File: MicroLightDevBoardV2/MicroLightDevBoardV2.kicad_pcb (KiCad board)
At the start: 2 copper layers, 58 parts, among them J1 Conn_01x05_Socket, J10 Conn_01x01_Socket, J11 Conn_01x04_Socket, J12 Conn_01x05_Socket, J13 Conn_01x02_Socket, J14 Conn_01x04_Socket, J15 Conn_01x04_Socket, J16 Conn_01x05_Socket, J17 Conn_01x01_Socket, J18 Conn_01x03_Socket, J19 Conn_01x03_Socket, J2 Conn_01x05_Socket, J20 Conn_01x02_Socket, J21 Conn_01x02_Socket, J22 Conn_01x02_Socket, J23 Conn_01x02_Socket, J24 Conn_01x01_Socket, J25 Conn_01x06_Socket, J26 Conn_01x04_Socket, J3 Conn_01x05_Socket, J4 Conn_01x05_Socket, J5 Conn_01x02_Socket, J6 Conn_01x02_Socket, J7 TYPE-C-31-M-12, J8 Conn_01x02_Socket, J9 Conn_01x02_Socket, U1 BQ25628RYKR, U2 ATtiny3226-M, U3 S-85S1AB33-I6T1U, U4 USBLC6-2P6, U5 MC3479

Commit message: organizing on pcb
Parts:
- moved J12 41.3 mm to (132.3, 30.7)
- moved J15 35.2 mm to (128.1, 44.9), turned to 90 degrees
- moved J17 33.8 mm to (153.9, 44.7)
- moved J5 33.1 mm to (151.4, 36.1), turned to 90 degrees
- moved R2 28.7 mm to (145.9, 37.2)
- moved R3 26.6 mm to (146.0, 39.7)
- moved J6 26.3 mm to (151.4, 39.8), turned to 90 degrees
- moved U1 26.2 mm to (131.4, 39.7)
- moved C4 26.0 mm to (137.2, 39.7), turned to -90 degrees
- moved C1 24.3 mm to (128.3, 38.0), turned to -90 degrees
- moved C3 24.0 mm to (135.7, 39.7), turned to -90 degrees
- moved R1 23.2 mm to (145.9, 42.3)
- moved J13 23.2 mm to (123.4, 30.7), turned to 90 degrees
- moved J14 21.9 mm to (123.4, 35.8)
- moved J16 14.1 mm to (142.6, 34.6)
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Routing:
- net GND_CHRG: track 0.00 -> 53.5 mm, vias 0 -> 2
- net VREF_CHRG: track 0.00 -> 32.7 mm
- net SCL_CHRG: track 0.00 -> 20.3 mm, vias 0 -> 1
- net SDA_CHRG: track 0.00 -> 19.4 mm
- net INT: track 0.00 -> 13.2 mm, vias 0 -> 1
- net SYS: track 0.00 -> 13.1 mm
- net VBUS_CHRG: track 0.00 -> 12.5 mm
- net STAT: track 0.00 -> 11.9 mm, vias 0 -> 1
- net CE: track 0.00 -> 11.7 mm, vias 0 -> 1
- net SW: track 0.00 -> 11.4 mm
- net BAT: track 0.00 -> 10.6 mm, vias 0 -> 2
- net PMID: track 0.00 -> 10.5 mm
- net REGN: track 0.00 -> 8.06 mm
- net TS_BIAS: track 0.00 -> 7.87 mm
- net PMID_GO: track 0.00 -> 7.18 mm
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
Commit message: organizing on pcb, acl
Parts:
- moved J20 89.0 mm to (130.1, 54.7), turned to -90 degrees
- moved J23 78.2 mm to (130.1, 73.1), turned to -90 degrees
- moved R9 69.3 mm to (128.9, 57.4), turned to 180 degrees
- moved J25 68.2 mm to (135.8, 57.5)
- moved C9 61.6 mm to (143.0, 63.2), turned to 90 degrees
- moved J19 60.0 mm to (145.8, 60.4), turned to 90 degrees
- moved R10 58.4 mm to (128.9, 58.9), turned to 180 degrees
- moved R12 53.0 mm to (128.9, 70.4), turned to 180 degrees
- moved R11 52.2 mm to (128.9, 68.8), turned to 180 degrees
- moved J22 49.7 mm to (130.1, 66.1), turned to -90 degrees
- moved J24 49.3 mm to (123.9, 63.8)
- moved U5 48.7 mm to (140.7, 63.2)
- moved J21 43.7 mm to (130.1, 61.6), turned to -90 degrees
- moved J18 43.7 mm to (150.9, 65.8), turned to -90 degrees
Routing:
- net INTN2_ACL: track 0.00 -> 24.3 mm, vias 0 -> 1
- net INTN1_ACL: track 0.00 -> 24.0 mm, vias 0 -> 1
- net SCK_SCL_ACL: track 0.00 -> 19.6 mm
- net DIN_SDA_ACL: track 0.00 -> 19.3 mm, vias 0 -> 1
- net GND_ACL: track 0.00 -> 10.7 mm
- net VDD_ACL: track 0.00 -> 10.5 mm
- net DOUT_A6: track 0.00 -> 4.81 mm
- net CSN: track 0.00 -> 4.31 mm
- added copper zone on F.Cu, net VREF_ACL

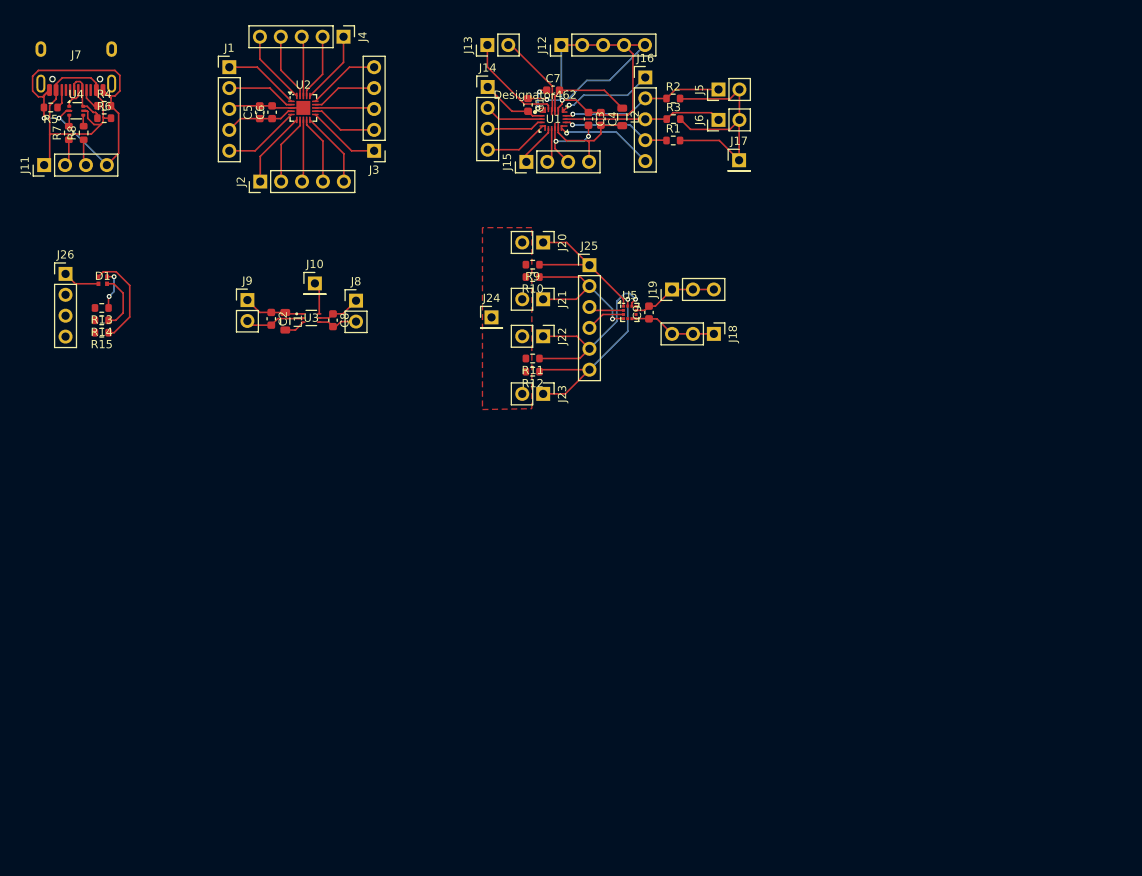
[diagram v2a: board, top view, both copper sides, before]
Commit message: add power lanes
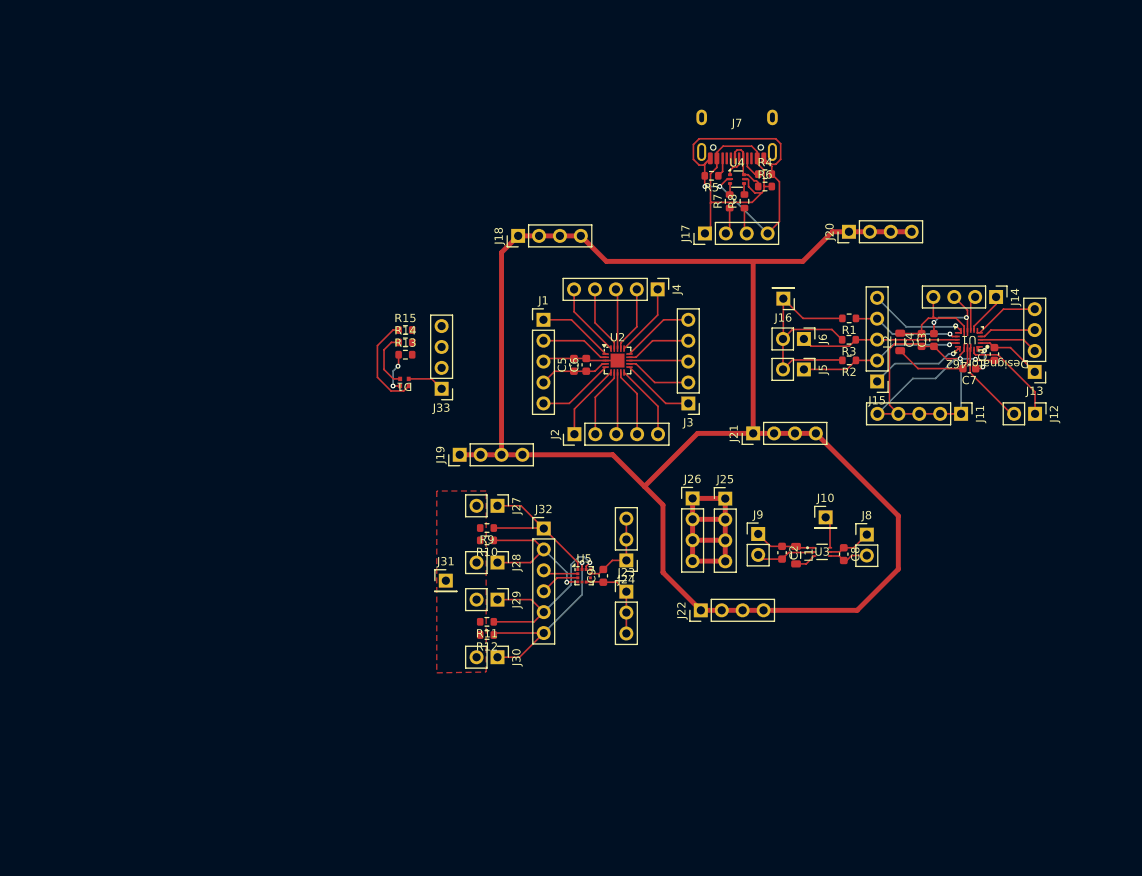
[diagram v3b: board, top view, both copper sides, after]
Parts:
- added J18: Conn_01x04_Socket, Connector_PinHeader_2.54mm:PinHeader_1x04_P2.54mm_Vertical, F.Cu at (127.1, 53.9)
- added J19: Conn_01x04_Socket, Connector_PinHeader_2.54mm:PinHeader_1x04_P2.54mm_Vertical, F.Cu at (120.0, 80.5)
- added J20: Conn_01x04_Socket, Connector_PinHeader_2.54mm:PinHeader_1x04_P2.54mm_Vertical, F.Cu at (167.3, 53.4)
- added J21: Conn_01x04_Socket, Connector_PinHeader_2.54mm:PinHeader_1x04_P2.54mm_Vertical, F.Cu at (155.7, 77.9)
- added J22: Conn_01x04_Socket, Connector_PinHeader_2.54mm:PinHeader_1x04_P2.54mm_Vertical, F.Cu at (149.3, 99.4)
- added J25: Conn_01x04_Socket, Connector_PinHeader_2.54mm:PinHeader_1x04_P2.54mm_Vertical, F.Cu at (152.3, 85.8)
- added J26: Conn_01x04_Socket, Connector_PinHeader_2.54mm:PinHeader_1x04_P2.54mm_Vertical, F.Cu at (148.3, 85.8)
- moved J17 80.7 mm to (149.8, 53.6)
- moved R7 80.7 mm to (152.8, 49.7)
- moved R4 80.7 mm to (157.1, 46.4)
- moved R5 80.7 mm to (150.6, 46.6)
- moved R6 80.7 mm to (157.1, 47.9)
- moved R8 80.7 mm to (154.6, 49.7)
- moved J7 80.7 mm to (153.7, 45.2)
- moved U4 80.7 mm to (153.7, 47.0)
- moved J12 80.2 mm to (189.9, 75.5), turned to -90 degrees
- moved J13 74.9 mm to (189.9, 70.4), turned to 180 degrees
- moved C2 68.3 mm to (159.2, 92.4)
- moved C8 68.3 mm to (166.7, 92.6)
- moved J10 68.3 mm to (164.5, 88.1)
- moved J8 68.3 mm to (169.5, 90.2)
- moved J9 68.3 mm to (156.3, 90.1)
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- renumbered J12 to J11, J13 to J12, J14 to J13, J15 to J14, J16 to J15, J17 to J16, J11 to J17, J18 to J23, J19 to J24, J20 to J27, J21 to J28, J22 to J29, J23 to J30, J24 to J31, J25 to J32, J26 to J33
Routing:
- net GND_LANE: track 0.00 -> 211.1 mm
- net 3.3V_LANE: track 0.00 -> 31.2 mm

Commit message: fix pin socket footprints
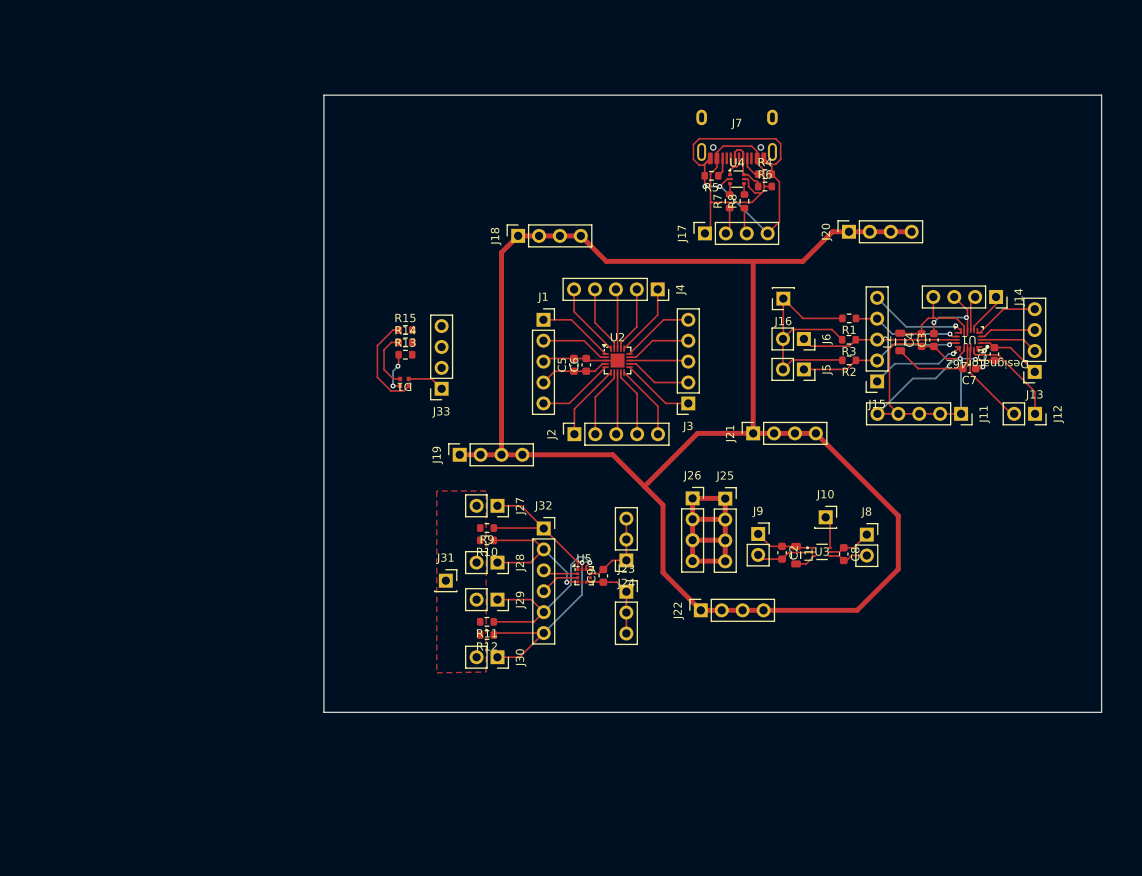
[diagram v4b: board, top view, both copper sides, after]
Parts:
- J1, J11, J15, J2, J3, J4: footprint Connector_PinHeader_2.54mm:PinHeader_1x05_P2.54mm_Vertical -> Connector_PinSocket_2.54mm:PinSocket_1x05_P2.54mm_Vertical
- J10, J16, J31: footprint Connector_PinHeader_2.54mm:PinHeader_1x01_P2.54mm_Vertical -> Connector_PinSocket_2.54mm:PinSocket_1x01_P2.54mm_Vertical
- J12, J27, J28, J29, J30, J5, J6, J8, J9: footprint Connector_PinHeader_2.54mm:PinHeader_1x02_P2.54mm_Vertical -> Connector_PinSocket_2.54mm:PinSocket_1x02_P2.54mm_Vertical
- J13, J14, J17, J18, J19, J20, J21, J22, J25, J26, J33: footprint Connector_PinHeader_2.54mm:PinHeader_1x04_P2.54mm_Vertical -> Connector_PinSocket_2.54mm:PinSocket_1x04_P2.54mm_Vertical
- J23, J24: footprint Connector_PinHeader_2.54mm:PinHeader_1x03_P2.54mm_Vertical -> Connector_PinSocket_2.54mm:PinSocket_1x03_P2.54mm_Vertical
- J32: footprint Connector_PinHeader_2.54mm:PinHeader_1x06_P2.54mm_Vertical -> Connector_PinSocket_2.54mm:PinSocket_1x06_P2.54mm_Vertical
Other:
- board outline added: 94.5 x 75 mm

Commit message: fixed silkscreen warnings/errors
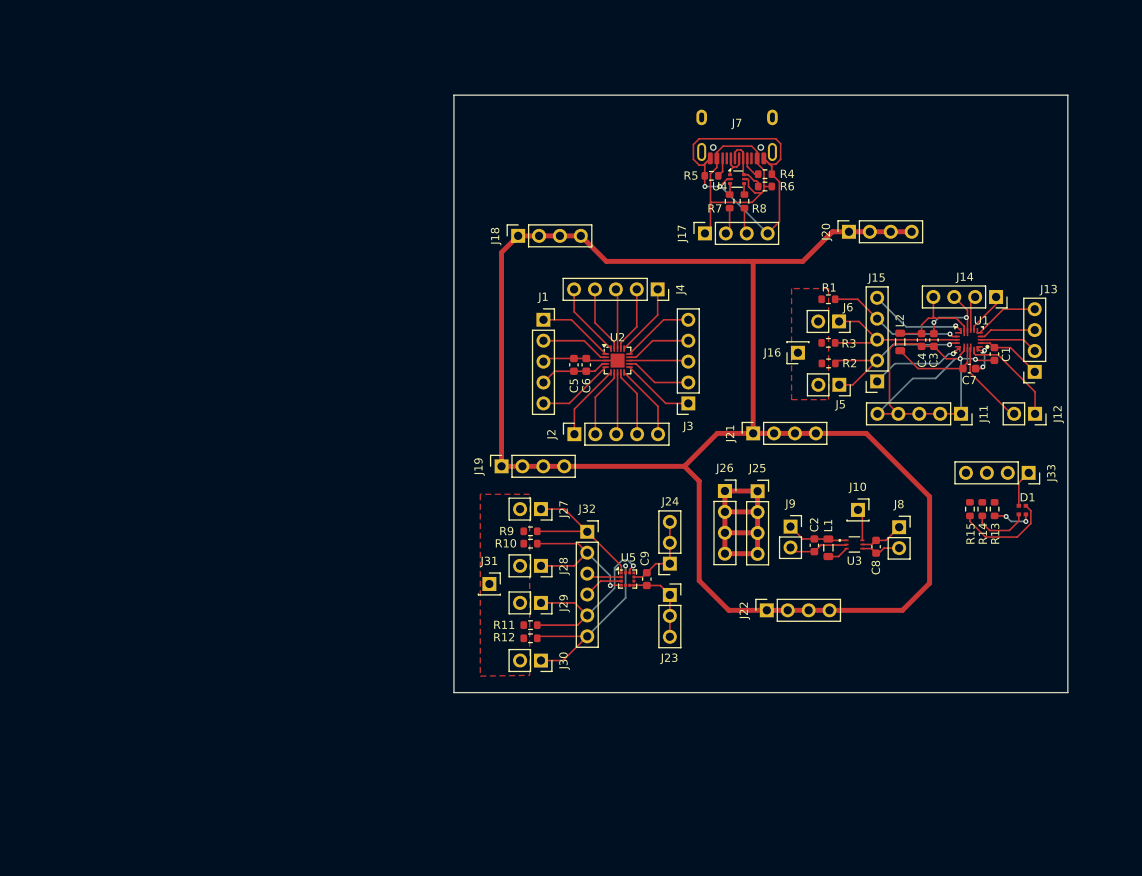
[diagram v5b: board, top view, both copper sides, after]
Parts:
- moved D1 76.7 mm to (188.4, 87.2), turned to -90 degrees
- moved R13 74.0 mm to (185.0, 87.1), turned to 90 degrees
- moved R14 73.0 mm to (183.5, 87.1), turned to 90 degrees
- moved J33 72.1 mm to (189.1, 82.7), turned to -90 degrees
- moved R15 72.0 mm to (182.0, 87.1), turned to 90 degrees
- moved J22 8.02 mm to (157.3, 99.4)
- moved J16 6.81 mm to (161.1, 68.1)
- moved C9 5.30 mm to (142.7, 95.6)
- moved J24 5.30 mm to (145.5, 93.7)
- moved J28 5.30 mm to (129.9, 94.0)
- moved J29 5.30 mm to (129.9, 98.5)
- moved J30 5.30 mm to (129.9, 105.5)
- moved J31 5.30 mm to (123.6, 96.2)
- moved J32 5.30 mm to (135.5, 89.9)
- moved R11 5.30 mm to (128.6, 101.2)
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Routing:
- net VREF_CHRG: track 32.7 -> 0.00 mm
- net INT: track 13.2 -> 16.7 mm
- net GND_LANE: track 211.1 -> 213.3 mm
- net SCL_CHRG: track 20.3 -> 22.0 mm
- net SDA_CHRG: track 19.4 -> 20.6 mm
- added copper zone on F.Cu, net VREF_CHRG
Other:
- board size 94.5 x 75 mm -> 74.6 x 72.6 mm

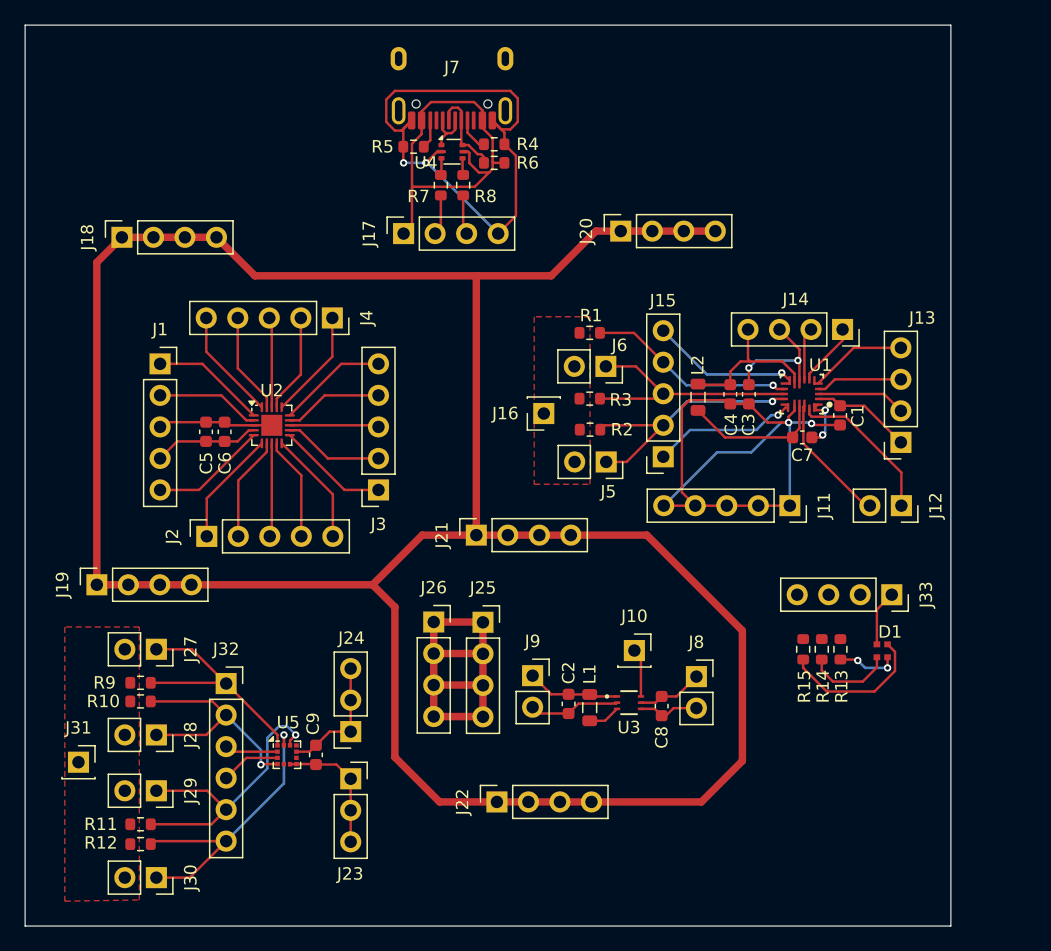
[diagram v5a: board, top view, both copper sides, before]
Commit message: added pin labels to silk screen
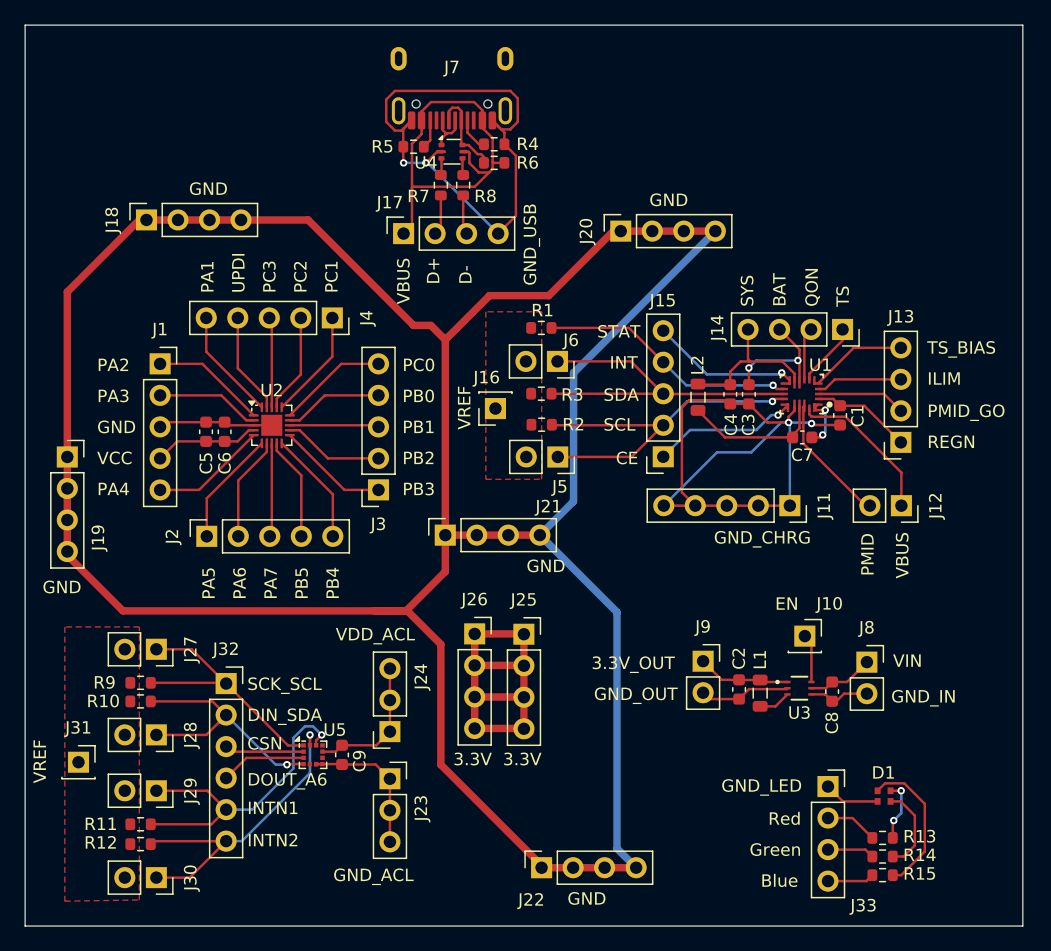
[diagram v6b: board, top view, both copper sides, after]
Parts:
- moved R15 19.3 mm to (188.4, 105.3), turned to 180 degrees
- moved R14 17.4 mm to (188.4, 103.8), turned to 180 degrees
- moved J33 16.3 mm to (184.0, 98.2), turned to 0 degrees
- moved R13 15.6 mm to (188.4, 102.3), turned to 180 degrees
- moved C2 13.8 mm to (176.8, 90.3)
- moved C8 13.8 mm to (184.3, 90.5)
- moved J10 13.8 mm to (182.1, 86.0)
- moved J8 13.8 mm to (187.1, 88.1)
- moved J9 13.8 mm to (173.9, 88.1)
- moved L1 13.8 mm to (178.5, 90.6)
- moved U3 13.8 mm to (181.7, 90.2)
- moved D1 11.7 mm to (188.5, 98.9), turned to 0 degrees
- moved J19 10.6 mm to (122.7, 71.6), turned to 0 degrees
- moved J22 6.41 mm to (160.9, 104.7)
- moved J5 3.92 mm to (162.2, 71.6)
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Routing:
- net GND_LANE: track 213.3 -> 239.2 mm
- net SDA_CHRG: track 20.6 -> 28.4 mm
- net SCL_CHRG: track 22.0 -> 29.5 mm
- net CaseRed: track 0.00 -> 4.24 mm
- net INT: track 16.7 -> 20.8 mm
- net CaseGreen: track 0.00 -> 3.81 mm
- net CaseBlue: track 0.00 -> 3.77 mm
- net DOUT_A6: track 4.81 -> 6.91 mm
- net CSN: track 4.31 -> 6.41 mm
- net INTN1_ACL: track 24.0 -> 26.1 mm
- net INTN2_ACL: track 24.3 -> 26.0 mm
- net SCK_SCL_ACL: track 19.6 -> 21.2 mm
- net DIN_SDA_ACL: track 19.3 -> 20.7 mm
- net GND_ACL: track 10.5 -> 11.5 mm
- net VDD_ACL: track 10.1 -> 11.2 mm
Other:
- board size 74.6 x 72.6 mm -> 80.4 x 72.6 mm
- board text added: "3.3V"
- board text added: "3.3V_OUT"
- board text added: "BAT"
- board text added: "Blue"
- board text added: "CE"
- board text added: "CSN"
- board text added: "D+"
- board text added: "D-"
- board text added: "DIN_SDA"
- board text added: "DOUT_A6"
- board text added: "EN"
- board text added: "GND"
- board text added: "GND_ACL"
- board text added: "GND_CHRG"
- board text added: "GND_IN"
- board text added: "GND_LED"
- board text added: "GND_OUT"
- board text added: "GND_USB"
- board text added: "Green"
- board text added: "ILIM"
- board text added: "INT"
- board text added: "INTN1"
- board text added: "INTN2"
- board text added: "PA1"
- board text added: "PA2"
- board text added: "PA3"
- board text added: "PA4"
- board text added: "PA5"
- board text added: "PA6"
- board text added: "PA7"
- board text added: "PB0"
- board text added: "PB1"
- board text added: "PB2"
- board text added: "PB3"
- board text added: "PB4"
- board text added: "PB5"
- board text added: "PC0"
- board text added: "PC1"
- board text added: "PC2"
- board text added: "PC3"
- board text added: "PMID"
- board text added: "PMID_GO"
- board text added: "QON"
- board text added: "REGN"
- board text added: "Red"
- board text added: "SCK_SCL"
- board text added: "SCL"
- board text added: "SDA"
- board text added: "STAT"
- board text added: "SYS"
- board text added: "TS"
- board text added: "TS_BIAS"
- board text added: "UPDI"
- board text added: "VBUS"
- board text added: "VCC"
- board text added: "VDD_ACL"
- board text added: "VIN"
- board text added: "VREF"
